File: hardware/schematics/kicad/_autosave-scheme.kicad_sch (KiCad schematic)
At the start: 14 parts

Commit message: base schematics added
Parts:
- removed CD1: Data Connector, symbol Connector:Conn_01x02_Pin
- removed CW1: Power Connector, symbol Connector:Conn_01x02_Pin
- added CONN: Connector to Controller, symbol Connector:Conn_01x04_Pin
- added CONN: Connector to Plants, symbol Connector:Conn_01x04_Socket
- added POW: Power IN (5-6V), symbol Connector:Conn_01x02_Pin
- BAT: value Battery_Cell -> Battery 18650 3.7V
- REG: value TP4057 -> TP4056
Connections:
- net 5V: now also CONN.+5V (Pin_3)
- net GND: now also CONN.GND (Pin_4); no longer D1.5 (GND)
- net at REG.2 (IN-): now also POW.2 (Pin_2)
- net at REG.3 (BAT): now also BAT.1 (+), STEP.5 (IN)
- net at REG.4 (IN+): now also POW.1 (Pin_1)
- net at REG.6 (BAT-): now also BAT.2 (-), STEP.4 (IN-)
- net at STEP.1 (OUT+): now also C0.8 (VCC), CONTR.8 (3V3), CONTR.9 (5V), CONN.+5V (Pin_3)
- net at STEP.3 (OUT-): now also C0.5 (GND), CONTR.10 (GND), CONN.GND (Pin_4)
- net at D1.6 (A): now also CONN.A (Pin_1)
- net at D1.7 (B): now also CONN.B (Pin_2)
- net at C0.6 (A): now also CONN.A (Pin_1)
- net at C0.7 (B): now also CONN.B (Pin_2)
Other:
- moved on the sheet: BAT, C0, CONTR, SC1

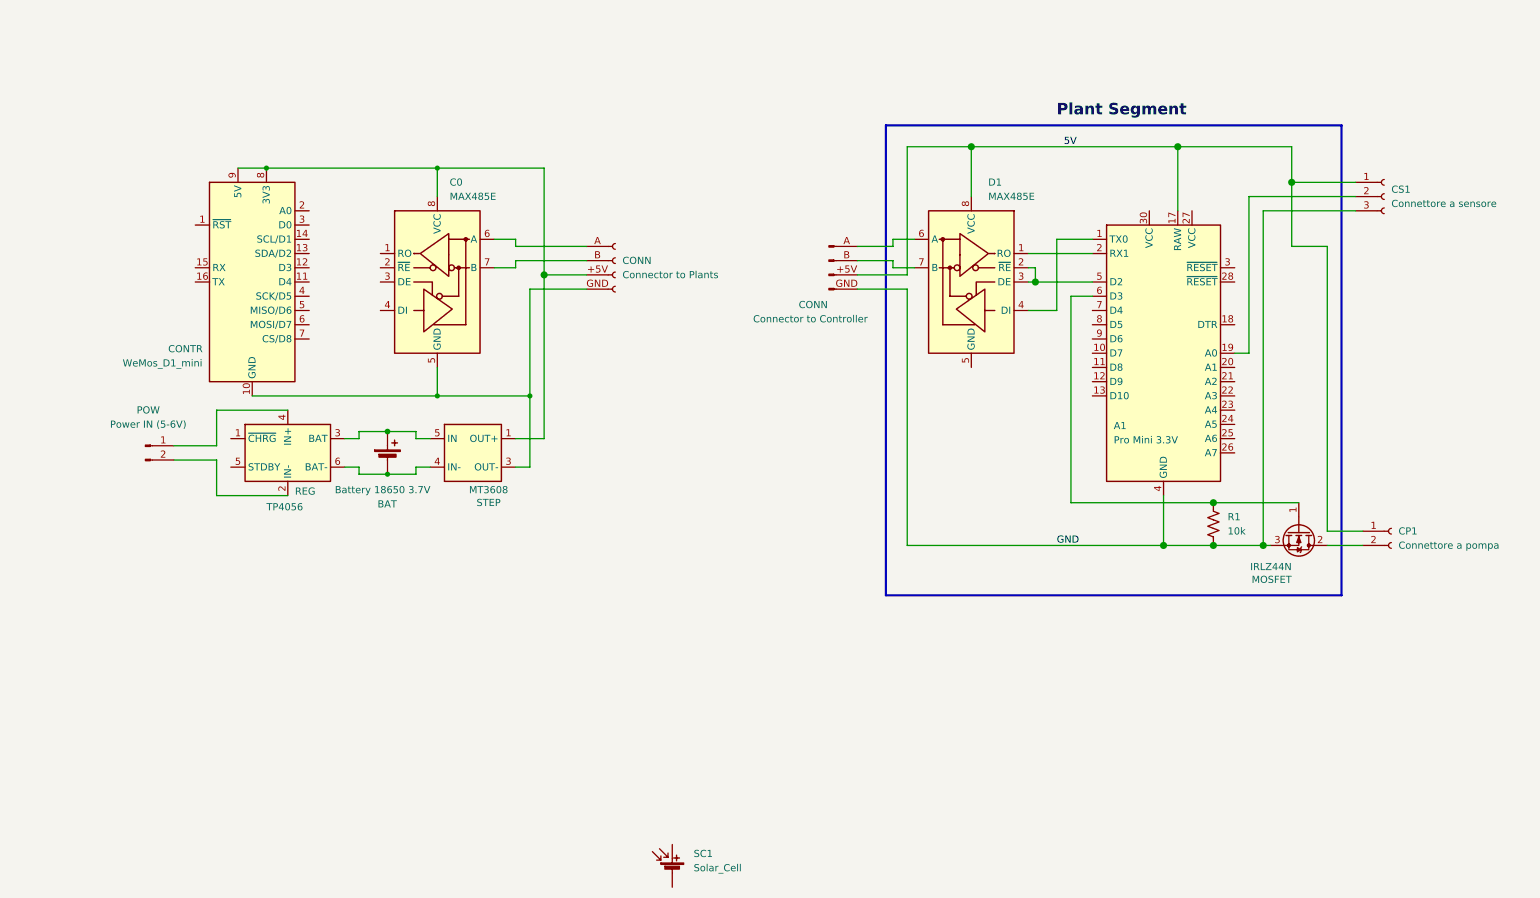
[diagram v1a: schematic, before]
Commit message: modified base schematics
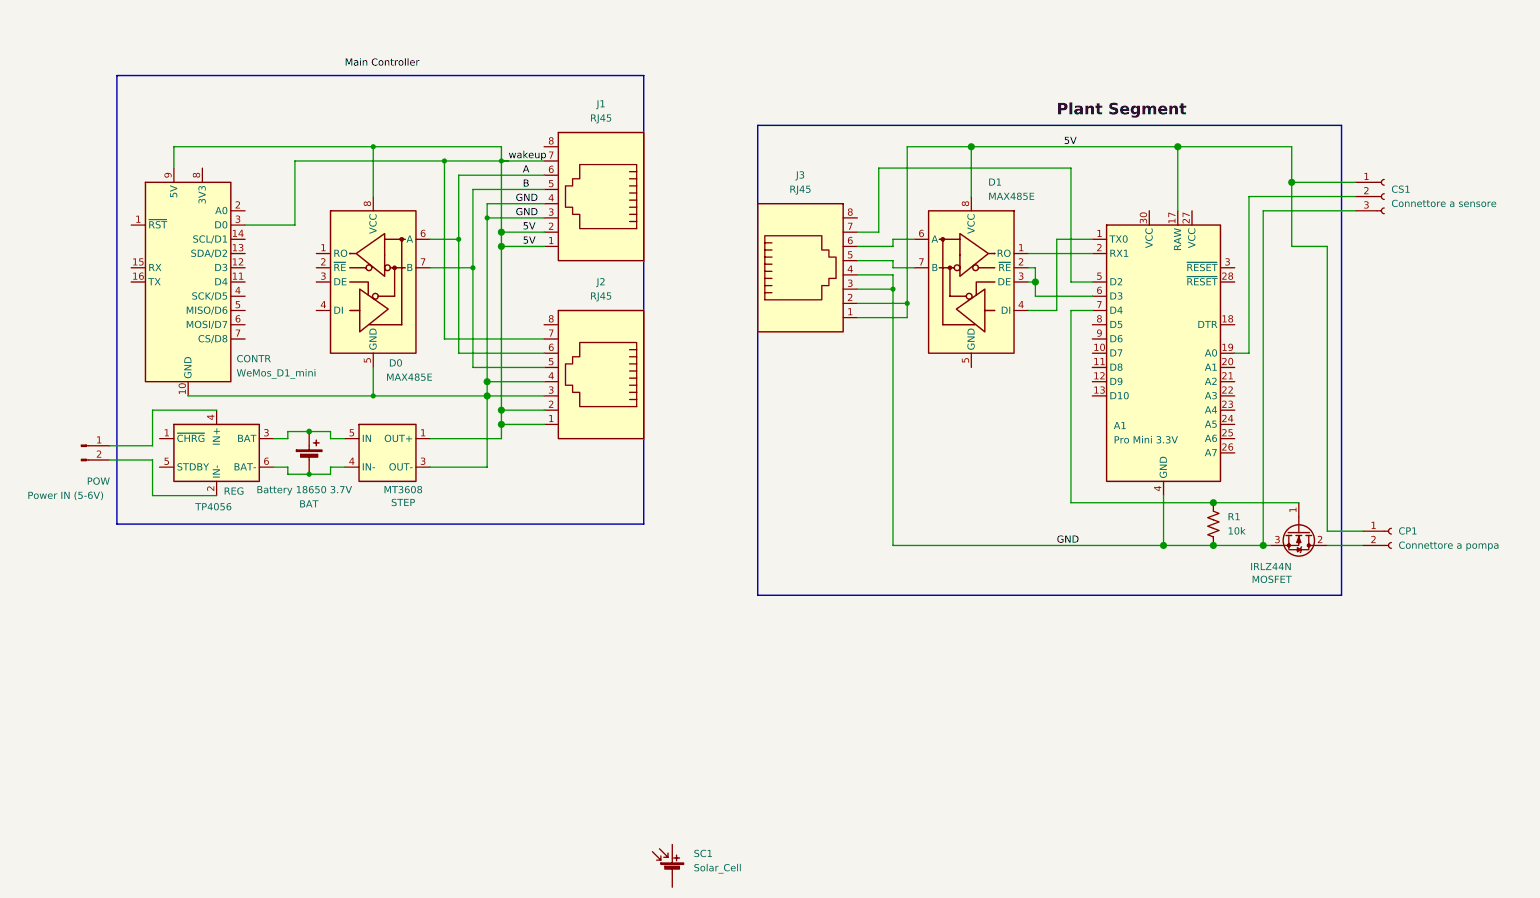
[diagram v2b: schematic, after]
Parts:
- removed CONN: Connector to Controller, symbol Connector:Conn_01x04_Pin
- removed CONN: Connector to Plants, symbol Connector:Conn_01x04_Socket
- added J1, J2, J3: RJ45, symbol Connector:RJ45
- renumbered C0 to D0
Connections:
- net 5V: now also CONTR.3 (D0), CONTR.9 (5V), D0.8 (VCC), STEP.1 (OUT+), J1.1, J1.2, J1.7, J2.1, J2.2, J2.7, J3.1, J3.2
- net GND: now also CONTR.10 (GND), D0.5 (GND), STEP.3 (OUT-), J1.3, J1.4, J2.3, J2.4, J3.3, J3.4
- net at D1.6 (A): now also J3.6
- net at D1.7 (B): now also J3.5
- net A: now reaches D0.6 (A)
- net A: now also J1.6, J2.6
- net B: now reaches D0.7 (B)
- net B: now also J1.5, J2.5
- net at D1.2 (~{RE}), D1.3 (DE): now also A1.6 (D3); no longer A1.5 (D2)
- net at MOSFET.1 (G), R1.1: now also A1.7 (D4); no longer A1.6 (D3)
- new net: A1.5 (D2), J3.7
- now unconnected: CONTR.8 (3V3)
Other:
- moved on the sheet: BAT, CONTR, D0, POW, REG, STEP
